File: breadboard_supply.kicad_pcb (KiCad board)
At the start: 4 copper layers, 54 x 100 mm, 184 parts, among them J1 USB_C_Receptacle_USB2.0, J2 Barrel_Jack_Switch, J3 ST-Link, J4 SHDN, J5 SHDN, J6 RAIL_POL, J7 OUTPUT, J8 RAIL_POL, J9 OUTPUT, K1 HFD4-3, K2 HFD4-3, Q1 AO4805, Q2 AO4805, Q3 DMG2302U, Q4 AO4805, Q5 DMG2302U, Q6 DMG2302U, SW1 Button, SW2 Button, SW3 Button, SW4 Button, SW5 Button, U1 USBLC6-2SC6, U10 MAX5400, U11 SL6206-33NR, U12 STM32F070RBT6, U13 GN1640T, U14 74LVC1G14, U15 74LVC1G14, U16 INA180A4, U17 INA180A4, U2 CYPD3177-24LQXQ, U3 DZDH0401DW, U4 INA180A4, U5 DZDH0401DW, U6 TPS54202DDC, U7 TPS54202DDC, U8 MAX5400, U9 TPS54202DDC, Y1 8MHz

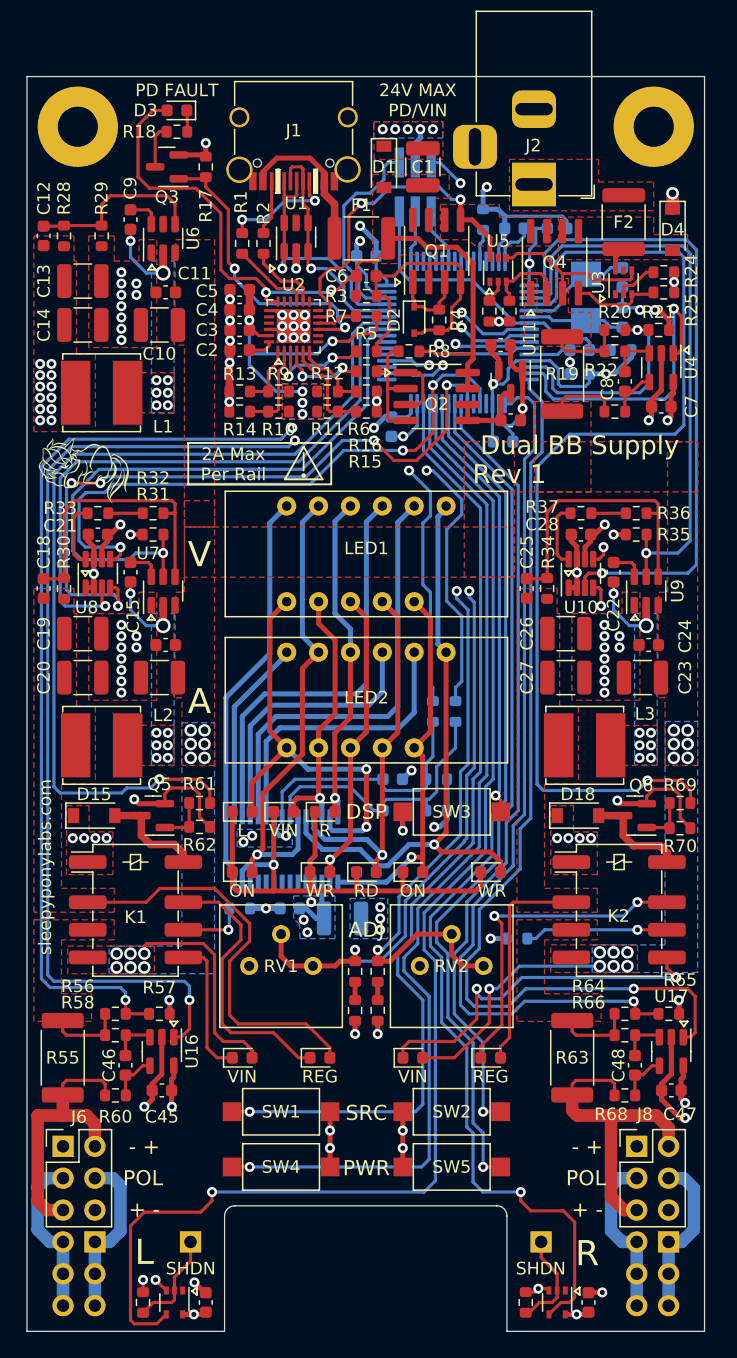
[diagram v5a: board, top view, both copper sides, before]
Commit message: Power optimization, add Aisler Assembly MPN info
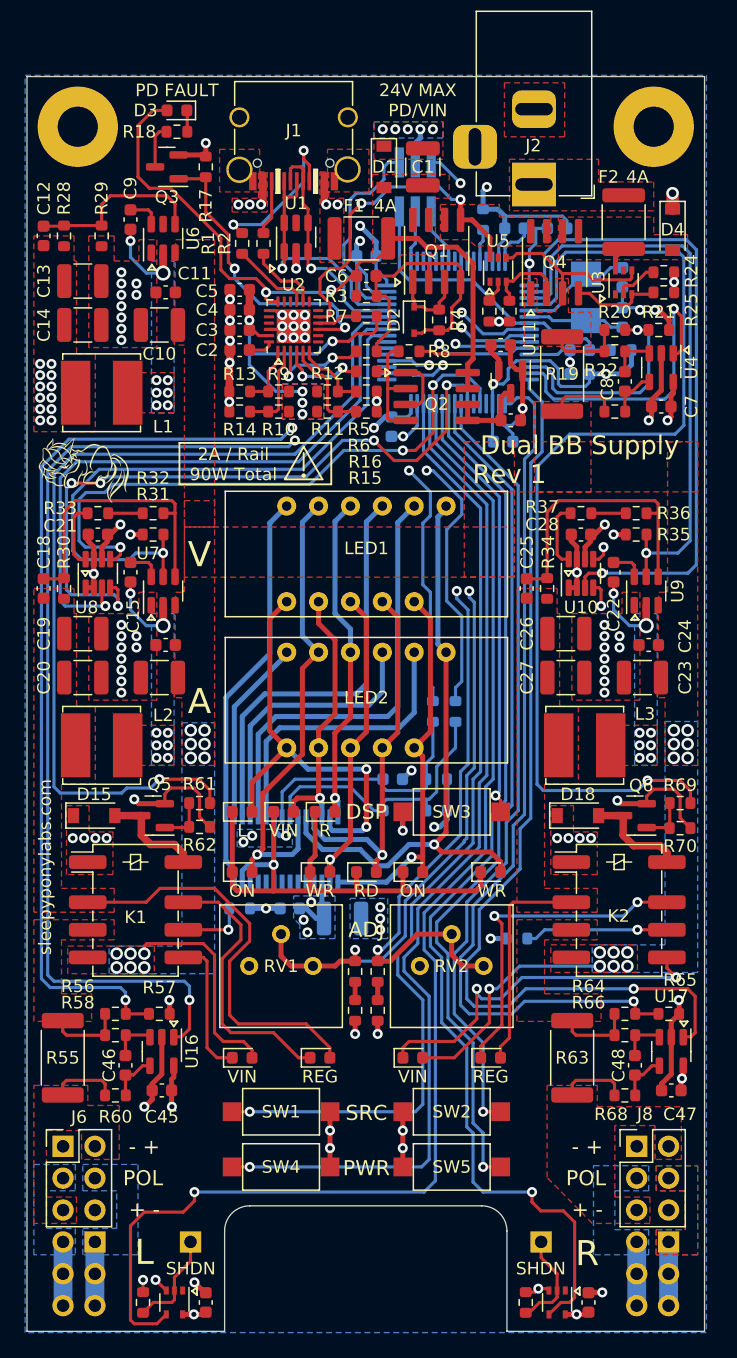
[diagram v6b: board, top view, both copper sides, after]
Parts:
- Q3, Q5, Q6: value DMG2302U -> SI2302
- R32, R36: value 3K3 -> 2K4
- R33, R37: value 680R -> 220R
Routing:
- net /Output Stage/ROUT: track 25.3 -> 5.40 mm
- net /Output Stage/LOUT: track 22.8 -> 5.40 mm
- net Net-(F1-Pad1): track 12.2 -> 3.83 mm, vias 0 -> 5
- net Net-(J8-Pad3): track 13.4 -> 5.08 mm
- net Net-(J6-Pad4): track 13.4 -> 5.08 mm
- net Net-(J6-Pad3): track 13.2 -> 5.08 mm
- net Net-(J8-Pad4): track 13.1 -> 5.08 mm
- net Net-(J1-PadA5): track 9.24 -> 13.1 mm
- net VBUS: track 61.4 -> 60.3 mm
- net GND: track 150.0 -> 148.9 mm, vias 89 -> 88
- net +3.3V: track 79.7 -> 78.9 mm
- added copper zone on F.Cu, net /Output Stage/LOUT
- added copper zone on In2.Cu, net /Output Stage/LOUT
- added copper zone on F.Cu, net /Output Stage/ROUT
- added copper zone on In2.Cu, net GND
- added copper zone on F.Cu, net Net-(F1-Pad1)
- added copper zone on In2.Cu, net Net-(F1-Pad1)
- added copper zone on B.Cu, net Net-(J6-Pad3)
- added copper zone on In1.Cu, net Net-(J6-Pad3)
- added copper zone on B.Cu, net Net-(J6-Pad4)
- added copper zone on B.Cu, net Net-(J8-Pad3)
- added copper zone on B.Cu, net Net-(J8-Pad4)
- added copper zone on F.Cu, net Net-(J8-Pad4)
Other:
- outline, holes or cut-outs redrawn
- board text added: "2A / Rail 90W Total"
- board text added: "4A"
- board text removed: "2A Max Per Rail"

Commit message: Fixed R7 value
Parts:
- R7: value 3K3 -> 2K4
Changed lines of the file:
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@@
       (effects (font (size 1 1) (thickness 0.15)))
     )
-    (fp_text value "3K3" (at 0 1.43) (layer "F.Fab")
+    (fp_text value "2K4" (at 0 1.43) (layer "F.Fab")
       (effects (font (size 1 1) (thickness 0.15)))
     )
